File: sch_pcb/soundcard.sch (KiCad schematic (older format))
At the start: 44 parts, among them U501 CM108B, U502 CM108B, U503 TUSB2036, Y501 6MHz

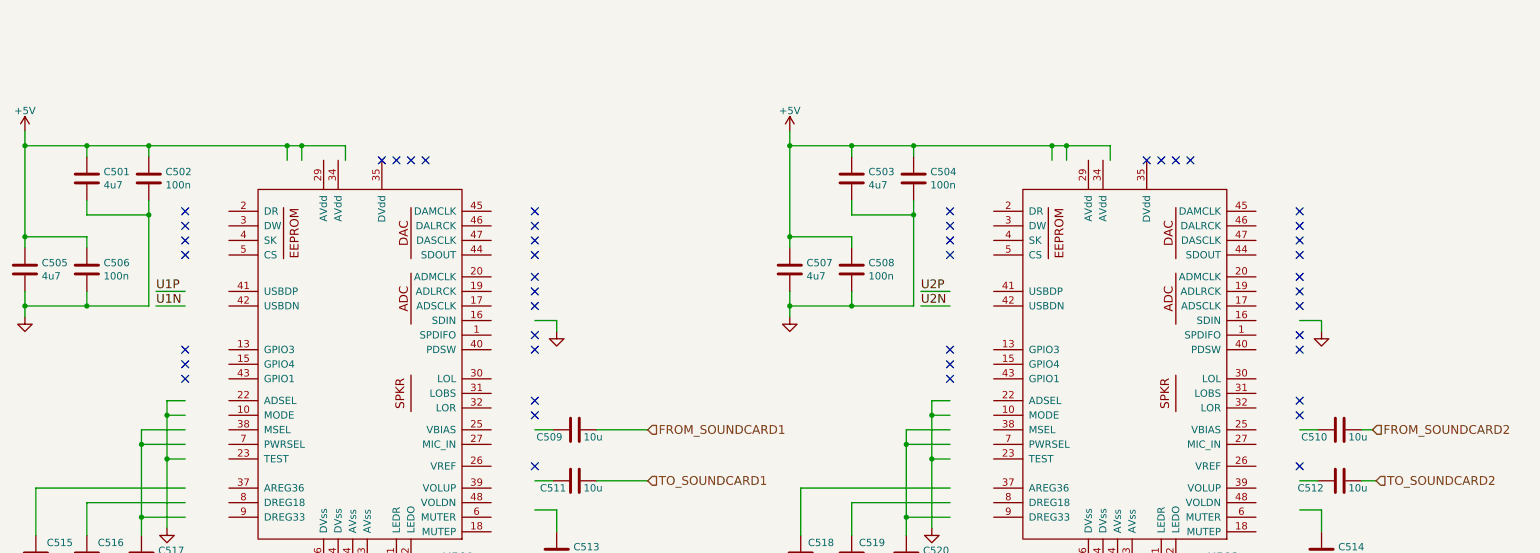
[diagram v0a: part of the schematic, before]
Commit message: Update to soundcard
Split AVdd and DVdd
Add caps and testpoints for right outputs
Move active outputs to left channel
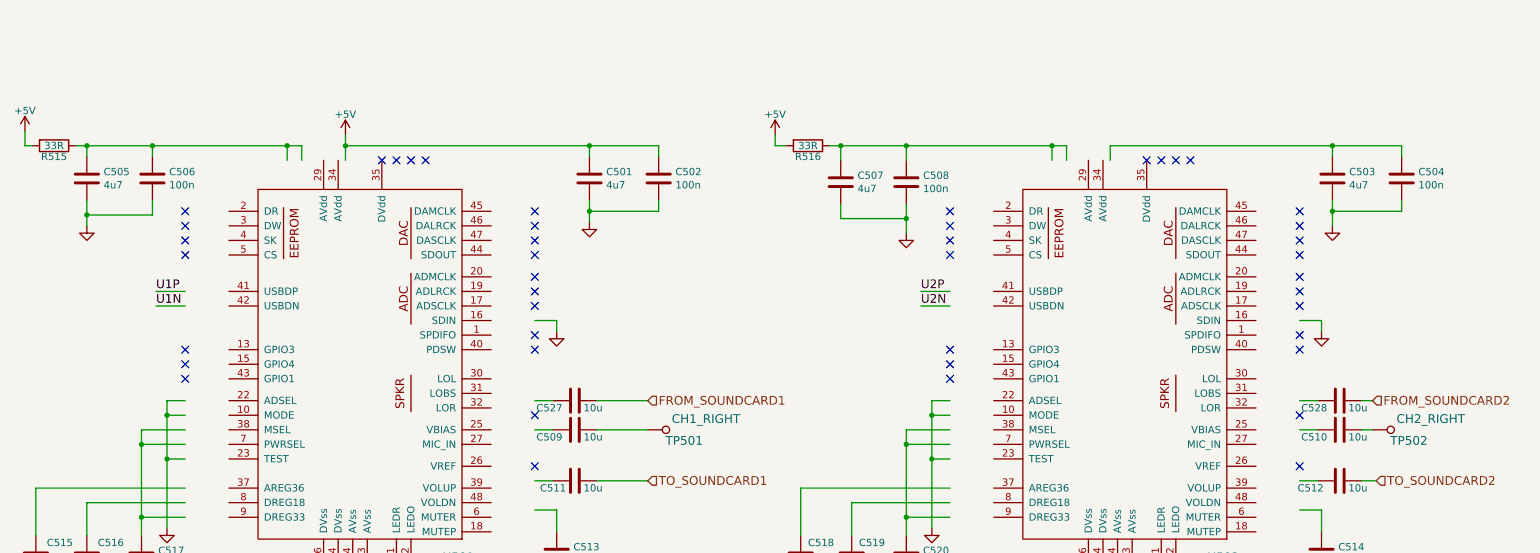
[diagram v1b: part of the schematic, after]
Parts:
- added C527, C528: 10u, lib:smd0603, symbol C
- added R515, R516: 33R, lib:smd0603, symbol R
- added TP501: CH1_RIGHT, symbol TESTPOINT
- added TP502: CH2_RIGHT, symbol TESTPOINT
- U501, U502: footprint Housings_QFP:LQFP-48_7x7mm_Pitch0.5mm -> lib:LQFP-48_7x7mm_Pitch0.5mm
- U503: footprint Housings_QFP:LQFP-32_7x7mm_Pitch0.8mm -> lib:LQFP-32_7x7mm_Pitch0.8mm
- Y501: footprint Crystals:Crystal_SMD_HC49-SD -> lib:Crystal_HC49-SD_SMD
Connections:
- wire segments 161 -> 169
- no-connect marks 58 -> 56
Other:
- moved on the sheet: C501, C502, C503, C504, C505, C506, C507, C508

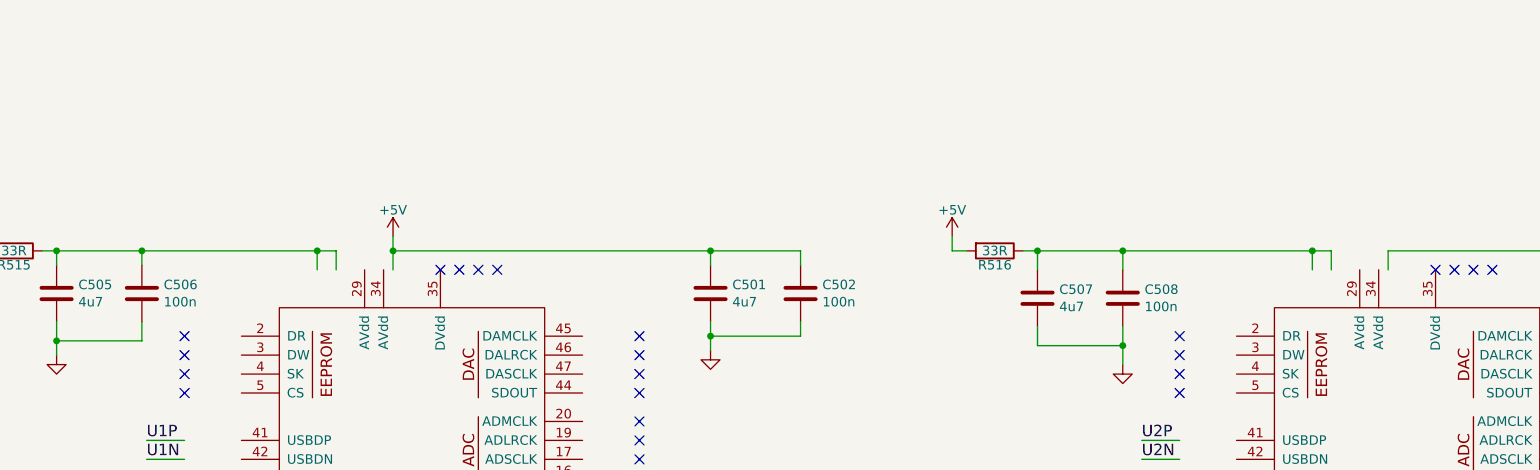
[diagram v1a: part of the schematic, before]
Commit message: Update from latest round of emails
Change connectors - use correct footprint for DE9F.  Add chassis connector as DE9M, AUX_IO connectors as 116-pin ribbon, expected to transition to DA15 with a cable.  
Remove screw terminals for 12V input as it now comes in on chassis connector
Remove third EEPOT package
Move stuff off PCB in preparation to incorporate all the schematic updates.
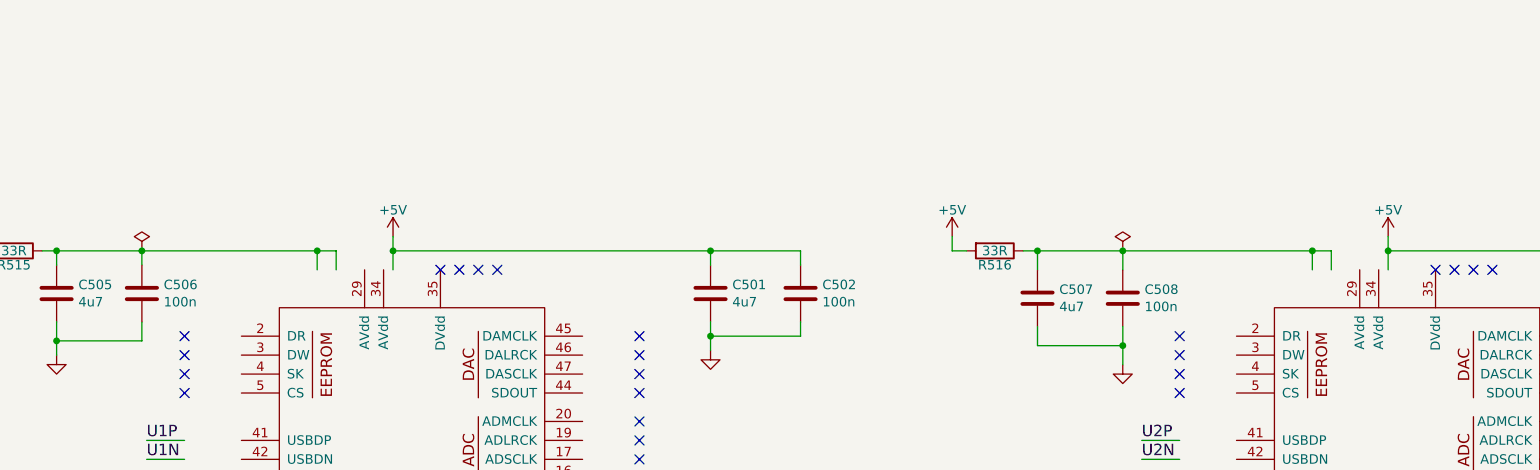
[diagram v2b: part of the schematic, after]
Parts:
- TP501, TP502: footprint (none) -> lib:Wire_28AWG
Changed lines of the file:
@@
 EESchema Schematic File Version 2
 LIBS:PiPtr
+LIBS:conn
 LIBS:PiPtr-cache
 EELAYER 25 0
@@
 	9775 2125 9775 2200
 $Comp
-L GND #PWR409
+L GND #PWR0149
 U 1 1 5968E48D
 P 9775 2200
-F 0 "#PWR409" H 9775 1950 50  0001 C CNN
+F 0 "#PWR0149" H 9775 1950 50  0001 C CNN
 F 1 "GND" H 9780 2027 50  0001 C CNN
 F 2 "" H 9775 2200 50  0001 C CNN
@@
 $EndComp
 $Comp
-L GND #PWR415
+L GND #PWR0150
 U 1 1 5968E4AC
 P 8575 4025
-F 0 "#PWR415" H 8575 3775 50  0001 C CNN
+F 0 "#PWR0150" H 8575 3775 50  0001 C CNN
 F 1 "GND" H 8580 3852 50  0001 C CNN
 F 2 "" H 8575 4025 50  0001 C CNN
@@
 Connection ~ 8275 3925
 $Comp
-L GND #PWR411
+L GND #PWR0151
 U 1 1 5968E5A1
 P 7100 3550
-F 0 "#PWR411" H 7100 3300 50  0001 C CNN
+F 0 "#PWR0151" H 7100 3300 50  0001 C CNN
 F 1 "GND" H 7105 3377 50  0001 C CNN
 F 2 "" H 7100 3550 50  0001 C CNN
@@
 	7925 925  7925 1025
 Wire Wire Line
-	8325 925  8325 1025
+	8325 850  8325 1025
 Connection ~ 7925 925
 Wire Wire Line
@@
 $EndComp
 $Comp
-L GND #PWR407
+L GND #PWR0152
 U 1 1 5968EB73
 P 6925 1525
-F 0 "#PWR407" H 6925 1275 50  0001 C CNN
+F 0 "#PWR0152" H 6925 1275 50  0001 C CNN
 F 1 "GND" H 6930 1352 50  0001 C CNN
 F 2 "" H 6925 1525 50  0001 C CNN
@@
 $EndComp
 $Comp
-L GND #PWR413
+L GND #PWR0153
 U 1 1 5968F4FA
 P 9775 3975
-F 0 "#PWR413" H 9775 3725 50  0001 C CNN
+F 0 "#PWR0153" H 9775 3725 50  0001 C CNN
 F 1 "GND" H 9780 3802 50  0001 C CNN
 F 2 "" H 9775 3975 50  0001 C CNN
@@
 Connection ~ 6200 4000
 $Comp
-L GND #PWR418
+L GND #PWR0154
 U 1 1 5968FE8C
 P 6200 4075
-F 0 "#PWR418" H 6200 3825 50  0001 C CNN
+F 0 "#PWR0154" H 6200 3825 50  0001 C CNN
 F 1 "GND" H 6205 3902 50  0001 C CNN
 F 2 "" H 6200 4075 50  0001 C CNN
@@
 	4525 2125 4525 2200
 $Comp
-L GND #PWR408
+L GND #PWR0155
 U 1 1 596926E6
 P 4525 2200
-F 0 "#PWR408" H 4525 1950 50  0001 C CNN
+F 0 "#PWR0155" H 4525 1950 50  0001 C CNN
 F 1 "GND" H 4530 2027 50  0001 C CNN
 F 2 "" H 4525 2200 50  0001 C CNN
@@
 $EndComp
 $Comp
-L GND #PWR414
+L GND #PWR0156
 U 1 1 596926EC
 P 3325 4025
-F 0 "#PWR414" H 3325 3775 50  0001 C CNN
+F 0 "#PWR0156" H 3325 3775 50  0001 C CNN
 F 1 "GND" H 3330 3852 50  0001 C CNN
 F 2 "" H 3325 4025 50  0001 C CNN
@@
 Connection ~ 3025 3925
 $Comp
-L GND #PWR410
+L GND #PWR0157
 U 1 1 596926FD
 P 1850 3550
-F 0 "#PWR410" H 1850 3300 50  0001 C CNN
+F 0 "#PWR0157" H 1850 3300 50  0001 C CNN
 F 1 "GND" H 1855 3377 50  0001 C CNN
 F 2 "" H 1850 3550 50  0001 C CNN
@@
 $EndComp
 $Comp
-L GND #PWR412
+L GND #PWR0158
 U 1 1 5969275D
 P 4525 3975
-F 0 "#PWR412" H 4525 3725 50  0001 C CNN
+F 0 "#PWR0158" H 4525 3725 50  0001 C CNN
 F 1 "GND" H 4530 3802 50  0001 C CNN
 F 2 "" H 4525 3975 50  0001 C CNN
@@
 Connection ~ 950  4000
 $Comp
-L GND #PWR416
+L GND #PWR0159
 U 1 1 59692791
 P 950 4075
-F 0 "#PWR416" H 950 3825 50  0001 C CNN
+F 0 "#PWR0159" H 950 3825 50  0001 C CNN
 F 1 "GND" H 955 3902 50  0001 C CNN
 F 2 "" H 950 4075 50  0001 C CNN
@@
 $EndComp
 $Comp
-L GND #PWR427
+L GND #PWR0160
 U 1 1 59695E9D
 P 1750 7675
-F 0 "#PWR427" H 1750 7425 50  0001 C CNN
+F 0 "#PWR0160" H 1750 7425 50  0001 C CNN
 F 1 "GND" H 1755 7502 50  0001 C CNN
 F 2 "" H 1750 7675 50  0001 C CNN
@@
 NoConn ~ 2600 6500
 $Comp
-L +3.3V #PWR422
+L +3.3V #PWR0161
 U 1 1 596973F4
 P 2450 5675
-F 0 "#PWR422" H 2450 5525 50  0001 C CNN
+F 0 "#PWR0161" H 2450 5525 50  0001 C CNN
 F 1 "+3.3V" H 2465 5848 50  0000 C CNN
 F 2 "" H 2450 5675 50  0001 C CNN
@@
 $EndComp
 $Comp
-L GND #PWR425
+L GND #PWR0162
 U 1 1 596977E6
 P 2525 6250
-F 0 "#PWR425" H 2525 6000 50  0001 C CNN
+F 0 "#PWR0162" H 2525 6000 50  0001 C CNN
 F 1 "GND" H 2530 6077 50  0001 C CNN
 F 2 "" H 2525 6250 50  0001 C CNN
@@
 $EndComp
 $Comp
-L GND #PWR423
+L GND #PWR0163
 U 1 1 596992AD
 P 2000 5900
-F 0 "#PWR423" H 2000 5650 50  0001 C CNN
+F 0 "#PWR0163" H 2000 5650 50  0001 C CNN
 F 1 "GND" H 2005 5727 50  0001 C CNN
 F 2 "" H 2000 5900 50  0001 C CNN
@@
 $EndComp
 $Comp
-L GND #PWR420
+L GND #PWR0164
 U 1 1 5969AB36
 P 4400 4400
-F 0 "#PWR420" H 4400 4150 50  0001 C CNN
+F 0 "#PWR0164" H 4400 4150 50  0001 C CNN
 F 1 "GND" H 4405 4227 50  0001 C CNN
 F 2 "" H 4400 4400 50  0001 C CNN
@@
 Connection ~ 3500 4325
 $Comp
-L +3.3V #PWR419
+L +3.3V #PWR0165
 U 1 1 5969B1EB
 P 3500 4250
-F 0 "#PWR419" H 3500 4100 50  0001 C CNN
+F 0 "#PWR0165" H 3500 4100 50  0001 C CNN
 F 1 "+3.3V" H 3515 4423 50  0000 C CNN
 F 2 "" H 3500 4250 50  0001 C CNN
@@
 Connection ~ 5750 6300
 $Comp
-L GND #PWR426
+L GND #PWR0166
 U 1 1 596A65D7
 P 5750 6375
-F 0 "#PWR426" H 5750 6125 50  0001 C CNN
+F 0 "#PWR0166" H 5750 6125 50  0001 C CNN
 F 1 "GND" H 5755 6202 50  0001 C CNN
 F 2 "" H 5750 6375 50  0001 C CNN
@@
 $EndComp
 $Comp
-L GND #PWR421
+L GND #PWR0167
 U 1 1 596AA48C
 P 2200 4900
-F 0 "#PWR421" H 2200 4650 50  0001 C CNN
+F 0 "#PWR0167" H 2200 4650 50  0001 C CNN
 F 1 "GND" H 2205 4727 50  0001 C CNN
 F 2 "" H 2200 4900 50  0001 C CNN
@@
 $EndComp
 $Comp
-L +3.3V #PWR417
+L +3.3V #PWR0168
 U 1 1 596AA4FD
 P 2200 4075
-F 0 "#PWR417" H 2200 3925 50  0001 C CNN
+F 0 "#PWR0168" H 2200 3925 50  0001 C CNN
 F 1 "+3.3V" H 2215 4248 50  0000 C CNN
 F 2 "" H 2200 4075 50  0001 C CNN
@@
 	4775 6125 4775 6050
 $Comp
-L +3.3V #PWR424
+L +3.3V #PWR0169
 U 1 1 5978D82E
 P 4775 6050
-F 0 "#PWR424" H 4775 5900 50  0001 C CNN
+F 0 "#PWR0169" H 4775 5900 50  0001 C CNN
 F 1 "+3.3V" H 4790 6223 50  0000 C CNN
 F 2 "" H 4775 6050 50  0001 C CNN
@@
 	10050 3225 10150 3225
 $Comp
-L +5V #PWR403
+L +5V #PWR0170
 U 1 1 597E7379
 P 6025 850
-F 0 "#PWR403" H 6025 700 50  0001 C CNN
+F 0 "#PWR0170" H 6025 700 50  0001 C CNN
 F 1 "+5V" H 6025 990 50  0000 C CNN
 F 2 "" H 6025 850 50  0001 C CNN
@@
 $EndComp
 $Comp
-L +5V #PWR401
+L +5V #PWR0171
 U 1 1 597E7689
 P 875 825
-F 0 "#PWR401" H 875 675 50  0001 C CNN
+F 0 "#PWR0171" H 875 675 50  0001 C CNN
 F 1 "+5V" H 875 965 50  0000 C CNN
 F 2 "" H 875 825 50  0001 C CNN
@@
 $EndComp
 $Comp
-L +5V #PWR402
+L +5V #PWR0172
 U 1 1 597C24B2
 P 3075 850
-F 0 "#PWR402" H 3075 700 50  0001 C CNN
+F 0 "#PWR0172" H 3075 700 50  0001 C CNN
 F 1 "+5V" H 3075 990 50  0000 C CNN
 F 2 "" H 3075 850 50  0001 C CNN
@@
 Connection ~ 9850 1375
 $Comp
-L GND #PWR406
+L GND #PWR0173
 U 1 1 597C4F1B
 P 9850 1475
-F 0 "#PWR406" H 9850 1225 50  0001 C CNN
+F 0 "#PWR0173" H 9850 1225 50  0001 C CNN
 F 1 "GND" H 9855 1302 50  0001 C CNN
 F 2 "" H 9850 1475 50  0001 C CNN
@@
 $EndComp
 $Comp
-L GND #PWR404
+L GND #PWR0174
 U 1 1 597C5606
 P 4750 1450
-F 0 "#PWR404" H 4750 1200 50  0001 C CNN
+F 0 "#PWR0174" H 4750 1200 50  0001 C CNN
 F 1 "GND" H 4755 1277 50  0001 C CNN
 F 2 "" H 4750 1450 50  0001 C CNN
@@
 Connection ~ 1300 925
 $Comp
-L GND #PWR405
+L GND #PWR0175
 U 1 1 597C7ACB
 P 1300 1475
-F 0 "#PWR405" H 1300 1225 50  0001 C CNN
+F 0 "#PWR0175" H 1300 1225 50  0001 C CNN
 F 1 "GND" H 1305 1302 50  0001 C CNN
 F 2 "" H 1300 1475 50  0001 C CNN
@@
 F 0 "TP501" H 5400 2800 60  0000 C CNN
 F 1 "CH1_RIGHT" H 5550 2950 60  0000 C CNN
-F 2 "" H 5150 2875 60  0000 C CNN
+F 2 "lib:Wire_28AWG" H 5150 2875 60  0001 C CNN
 F 3 "" H 5150 2875 60  0000 C CNN
 	1    5150 2875
@@
 F 0 "TP502" H 10375 2800 60  0000 C CNN
 F 1 "CH2_RIGHT" H 10525 2950 60  0000 C CNN
-F 2 "" H 10125 2875 60  0000 C CNN
+F 2 "lib:Wire_28AWG" H 10125 2875 60  0001 C CNN
 F 3 "" H 10125 2875 60  0000 C CNN
 	1    10125 2875
@@
 Wire Wire Line
 	2775 925  2775 1025
+$Comp
+L +5V #PWR0176
+U 1 1 5982DF1C
+P 8325 850
+F 0 "#PWR0176" H 8325 700 50  0001 C CNN
+F 1 "+5V" H 8325 990 50  0000 C CNN
+F 2 "" H 8325 850 50  0001 C CNN
+F 3 "" H 8325 850 50  0001 C CNN
+	1    8325 850
+	1    0    0    -1
+$EndComp
+Connection ~ 8325 925
+$Comp
+L PWR_FLAG #FLG0177
+U 1 1 5982F39E
+P 6925 925
+F 0 "#FLG0177" H 6925 1000 50  0001 C CNN
+F 1 "PWR_FLAG" H 6925 1099 50  0001 C CNN
+F 2 "" H 6925 925 50  0001 C CNN
+F 3 "" H 6925 925 50  0001 C CNN
+	1    6925 925
+	1    0    0    -1
+$EndComp
+$Comp
+L PWR_FLAG #FLG0178
+U 1 1 5982F5DB
+P 1750 925
+F 0 "#FLG0178" H 1750 1000 50  0001 C CNN
+F 1 "PWR_FLAG" H 1750 1099 50  0001 C CNN
+F 2 "" H 1750 925 50  0001 C CNN
+F 3 "" H 1750 925 50  0001 C CNN
+	1    1750 925
+	1    0    0    -1
+$EndComp
 $EndSCHEMATC
